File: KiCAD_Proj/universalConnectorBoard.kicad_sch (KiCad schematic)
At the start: 27 parts, among them IC1 RPI_Pico_EvaluationBoard, IC2 SN74LV4052ADR, J1 691401700003B, J2 Display1, J3 Display2, J4 RPI4, J5 Ledstrip2, J6 MUX3_UART, J7 MUX4_UART, J8 Ledstrip1, U3 TMC2209_MotorDriver, U4 TMC2209_MotorDriver

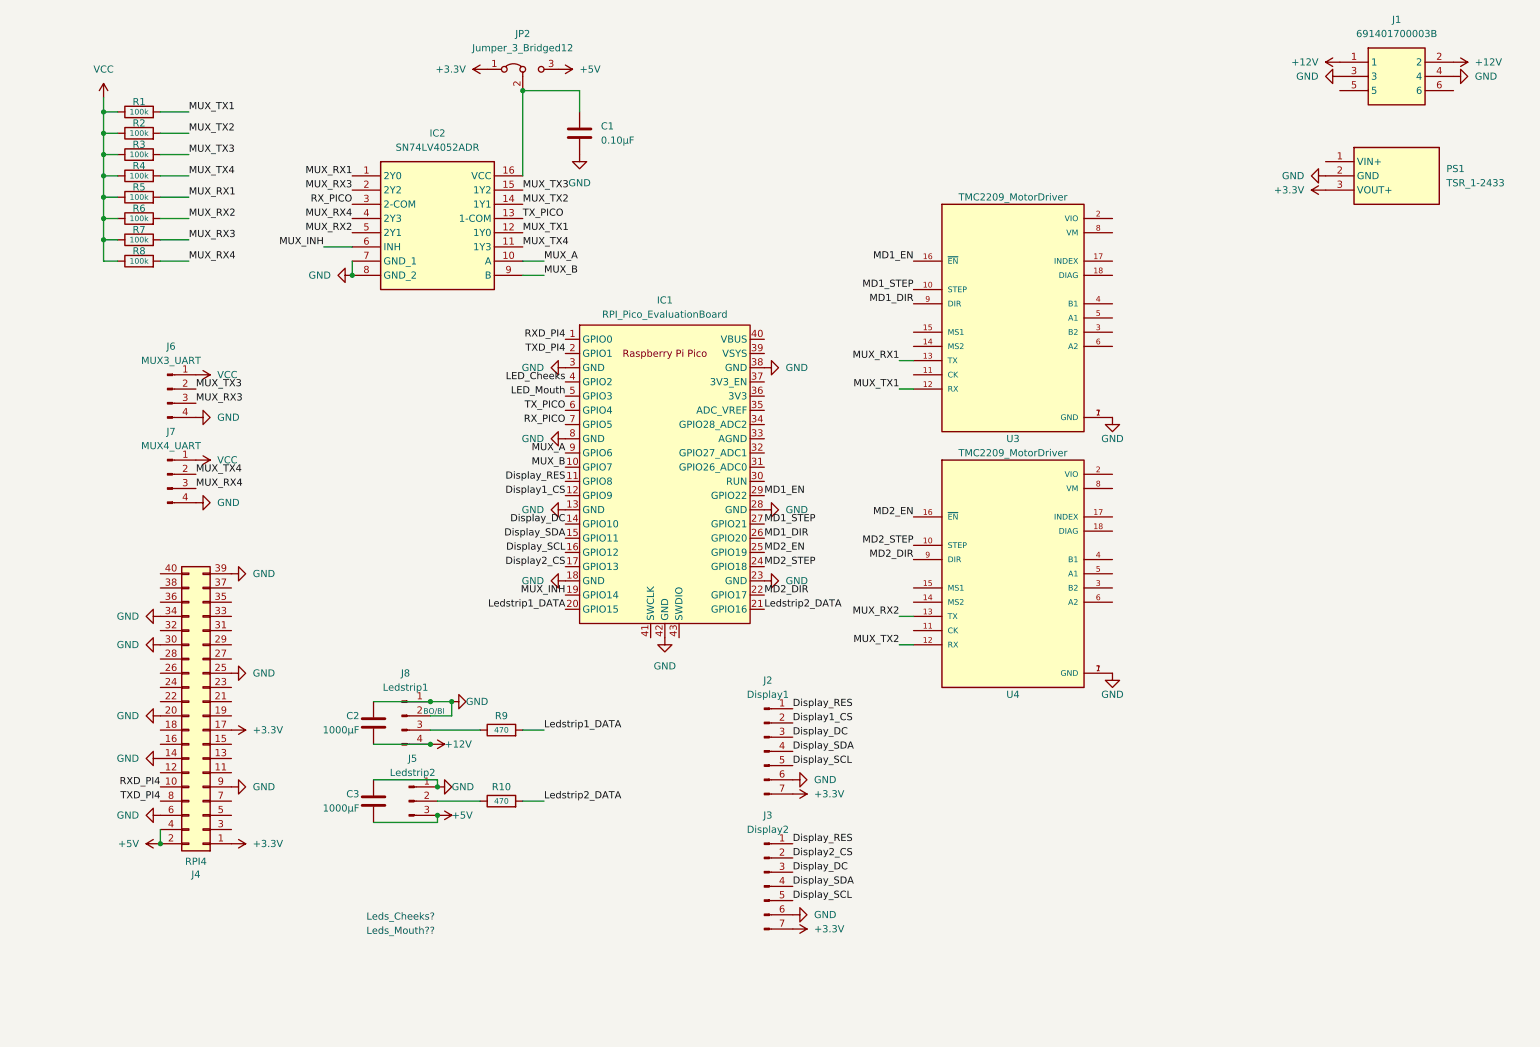
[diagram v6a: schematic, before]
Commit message: Added power management
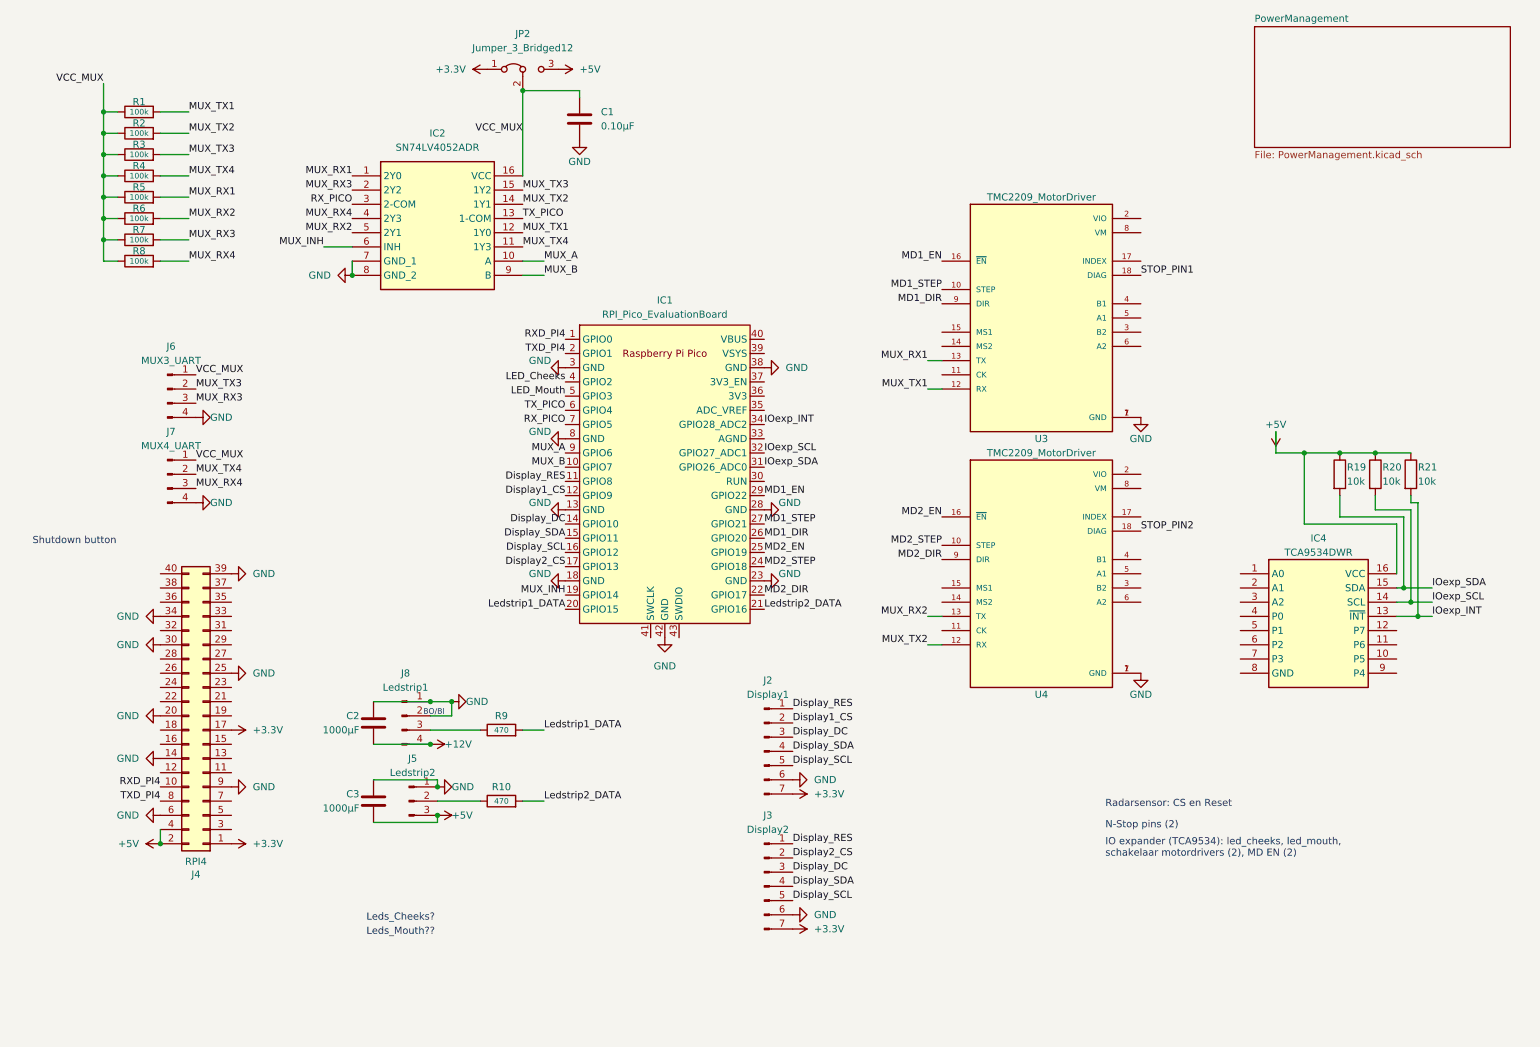
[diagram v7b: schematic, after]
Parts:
- removed J1: 691401700003B, SamacSys_Parts:691401700003B, symbol Healthbot-Symbols:Terminal_Block3
- removed PS1: TSR_1-2433, TSR-1-2433, symbol Healthbot-Symbols:DC-DC_3.3V
- added IC4: TCA9534DWR, SOIC127P1030X265-16N, symbol Healthbot-Symbols:TCA9534DWR_(I/O_expander)
- added R19, R20, R21: 10k, symbol Device:R
- IC2: footprint SOIC127P600X175-16N -> Healthbot-Footprints:SOIC127P600X175-16N
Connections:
- net VCC is gone; now on net VCC_MUX: J6.1 (Pin_1), J7.1 (Pin_1), R1.1, R2.1, R3.1, R4.1, R5.1, R6.1, R7.1, R8.1
- net +5V: now also IC4.16 (VCC), R19.1, R20.1, R21.1
- net VCC_MUX: now reaches C1.1, IC2.16 (VCC), JP2.2 (C)
- net STOP_PIN1: now reaches U3.18 (DIAG)
- net STOP_PIN2: now reaches U4.18 (DIAG)
- net IOexp_SDA: now reaches IC1.31 (GPIO26_ADC0)
- net IOexp_SDA: now also IC4.15 (SDA), R19.2
- net IOexp_SCL: now reaches IC1.32 (GPIO27_ADC1)
- net IOexp_SCL: now also IC4.14 (SCL), R20.2
- net IOexp_INT: now reaches IC1.34 (GPIO28_ADC2)
- net IOexp_INT: now also IC4.13 (~{INT}), R21.2
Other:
- added sheet PowerManagement (PowerManagement.kicad_sch)
- note added: "IO expander (TCA9534): led_cheeks, led_mouth, schakelaar motordrivers (2), MD EN (2)"
- note added: "N-Stop pins (2)"
- note added: "Radarsensor: CS en Reset"
- note added: "Shutdown button"
- moved on the sheet: C1, U3, U4

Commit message: Schematic nearly done, ordened
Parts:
- removed U3, U4: TMC2209_MotorDriver, TMC2209_SILENTSTEPSTICK:MODULE_TMC2209_SILENTSTEPSTICK, symbol projectLib:TMC2209_MotorDriver
- added J1: 691401700003B, SamacSys_Parts:691401700003B, symbol Healthbot-Symbols:Terminal_Block3
- added J10: Cheeks, Connector_JST:JST_XH_S2B-XH-A_1x02_P2.50mm_Horizontal, symbol Connector:Conn_01x02_Pin
- added J11: MD_SW1, Connector_JST:JST_XH_S2B-XH-A_1x02_P2.50mm_Horizontal, symbol Connector:Conn_01x02_Pin
- added J12: MD_SW2, Connector_JST:JST_XH_S2B-XH-A_1x02_P2.50mm_Horizontal, symbol Connector:Conn_01x02_Pin
- added J13: Motor1, Connector_JST:JST_XH_S6B-XH-A_1x06_P2.50mm_Horizontal, symbol Connector:Conn_01x06_Pin
- added J14: Motor2, Connector_JST:JST_XH_S6B-XH-A_1x06_P2.50mm_Horizontal, symbol Connector:Conn_01x06_Pin
- added J15: Conn_01x02_Pin, symbol Connector:Conn_01x02_Pin
- added J9: Mouth, Connector_JST:JST_XH_S2B-XH-A_1x02_P2.50mm_Horizontal, symbol Connector:Conn_01x02_Pin
- added PS1: TSR_1-2433, SamacSys_Parts:TSR-1-2433, symbol Healthbot-Symbols:DC-DC_3.3V
- added R22, R23: R, Resistor_SMD:R_0603_1608Metric_Pad0.98x0.95mm_HandSolder, symbol Device:R
- added R24, R25: 10k, Resistor_SMD:R_0603_1608Metric_Pad0.98x0.95mm_HandSolder, symbol Device:R
- IC4: footprint SOIC127P1030X265-16N -> SamacSys_Parts:SOIC127P1030X265-16N
- R19, R20, R21: footprint (none) -> Resistor_SMD:R_0603_1608Metric_Pad0.98x0.95mm_HandSolder
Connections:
- net +12V: now also J1.1, J1.2, PS1.1 (VIN+)
- net +3.3V: now also IC4.16 (VCC), R19.1, R20.1, R21.1, J11.2 (Pin_2), J12.2 (Pin_2), PS1.3 (VOUT+), R24.1, R25.1
- net +5V: no longer IC4.16 (VCC), R19.1, R20.1, R21.1
- net Display_DC: now also IC1.11 (GPIO8); no longer IC1.14 (GPIO10)
- net Display_RES: now also IC1.16 (GPIO12); no longer IC1.11 (GPIO8)
- net Display_SCL: now also IC1.15 (GPIO11); no longer IC1.16 (GPIO12)
- net Display_SDA: now also IC1.14 (GPIO10); no longer IC1.15 (GPIO11)
- net GND: now also IC4.1 (A0), IC4.2 (A1), IC4.3 (A2), IC4.8 (GND), J1.3, R22.1, R23.1, R24.2, R25.2
- net LED_Cheeks: now also IC4.10 (P5), J9.1 (Pin_1); no longer IC1.4 (GPIO2)
- net LED_Mouth: now also IC4.9 (P4), J10.1 (Pin_1); no longer IC1.5 (GPIO3)
- net MD1_EN: now also IC4.4 (P0); no longer IC1.29 (GPIO22)
- net MD1_STEP: now also IC1.25 (GPIO19); no longer IC1.27 (GPIO21)
- net MD2_DIR: now also IC1.29 (GPIO22); no longer IC1.22 (GPIO17)
- net MD2_EN: now also IC4.5 (P1); no longer IC1.25 (GPIO19)
- net MD2_STEP: now also IC1.27 (GPIO21); no longer IC1.24 (GPIO18)
- net STOP_PIN1: now also IC1.4 (GPIO2)
- net STOP_PIN2: now also IC1.5 (GPIO3)
- net MD_SW1: now reaches IC4.6 (P2)
- net MD_SW1: now also J11.1 (Pin_1)
- net MD_SW2: now reaches IC4.7 (P3)
- net MD_SW2: now also J12.1 (Pin_1)
- new net: J9.2 (Pin_2), R23.2
- new net: J10.2 (Pin_2), R22.2
- new net Radar_CS: IC1.22 (GPIO17)
- new net Radar_RES: IC1.24 (GPIO18)
- new net Regulator5V/GND: J1.4, PS1.2 (GND)
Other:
- sheet PowerManagement renamed Regulator5V
- added sheet StepperMotors (StepperMotors.kicad_sch)
- sheet Regulator5V ports: added 12V, 5V, GND; removed none
- note added: "2) Connectoren: leds, ledstrips, motoren 3) Shutdown button PI4? 4) 4,7 of 100k voor mux uart 5) Weerstandwaarde R22/R33 (kleur led?? 100/150) 6) Connector motoren? 4 of 6 pins"
- note added: "3.3V ?? 12V ??"
- note added: "4,7 of 100k?"
- note added: "COM"
- note added: "Display"
- note added: "Extra uart"
- note added: "I/O Expander"
- note added: "Leds head"
- note added: "Ledstrips"
- note added: "Limit Switches Motors"
- note added: "Motor management"
- note added: "NO"
- note added: "Power Management"
- note added: "Raspberry Pi Pico"
- note added: "Raspberry Pi4 pins"
- note added: "Shutdown button??"
- note added: "Vsys?"
- note removed: "IO expander (TCA9534): led_cheeks, led_mouth, schakelaar motordrivers (2), MD EN (2)"
- note removed: "Leds_Cheeks?"
- note removed: "Leds_Mouth??"
- note removed: "N-Stop pins (2)"
- note removed: "Radarsensor: CS en Reset"
- note removed: "Shutdown button"
- company: (none) -> HAN Univeristy of Applied Sciences
- title: (none) -> Project_Healthbot_HAT
- moved on the sheet: C2, C3, IC1, IC4, J2, J3, J4, J5, J6, J7, J8, R10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
